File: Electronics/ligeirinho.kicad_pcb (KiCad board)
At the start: 2 copper layers, 76.1 x 55.1 mm, 27 parts, among them J1 Bateria, J10 ponte H2, J11 VS1838B, J12 MPU6050, J13 ADNS-9500, J14 ADNS-9500 3V3, J2 ESP32 esq, J3 ESP32 dir, J4 VL53L0X 1, J5 VL53L0X 2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

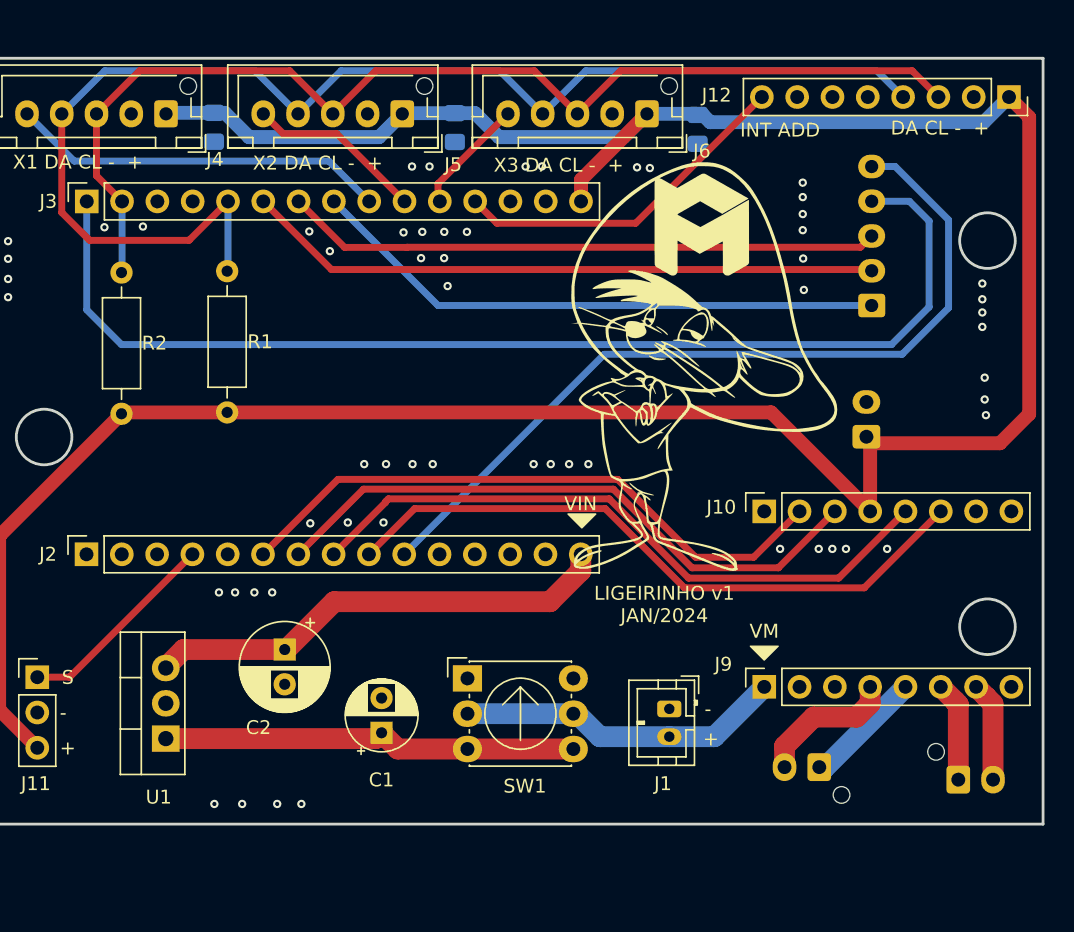
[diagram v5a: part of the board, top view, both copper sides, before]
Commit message: add: AMS1117 to 3v3 regulator
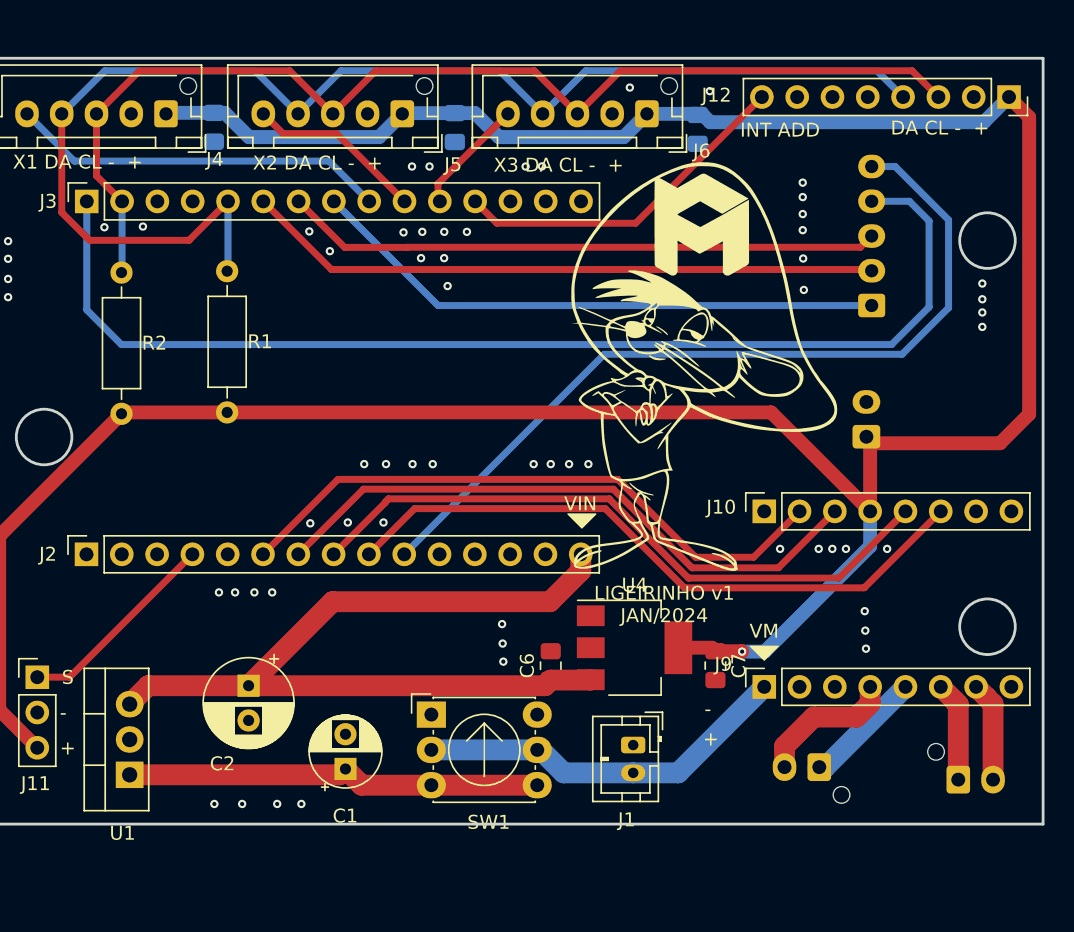
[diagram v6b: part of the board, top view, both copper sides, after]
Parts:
- added C6: 100nF, Capacitor_SMD:C_0805_2012Metric_Pad1.18x1.45mm_HandSolder, F.Cu at (195.1, 129.7)
- added C7: 10uF, Capacitor_SMD:C_0805_2012Metric_Pad1.18x1.45mm_HandSolder, F.Cu at (206.9, 129.7)
- added U4: AMS1117-3.3, Package_TO_SOT_SMD:SOT-223-3_TabPin2, F.Cu at (201.1, 128.4)
- moved J1 3.68 mm to (201.0, 135.4)
- moved C2 3.68 mm to (173.3, 131.1)
- moved U1 3.68 mm to (164.8, 137.6)
- moved C1 3.68 mm to (180.3, 137.1)
- moved SW1 3.68 mm to (186.5, 133.2)
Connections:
- J3 pad 15: 3V3 -> unconnected-(J3-Pin_15-Pad15)
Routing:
- net 5V: track 34.0 -> 62.4 mm
- net 3V3: track 199.0 -> 210.7 mm, vias 0 -> 1
- net 2s: track 23.5 -> 27.2 mm
- net GND: vias 56 -> 61
- net (no net): vias 2 -> 0

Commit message: fix: add some more stitching GND holes
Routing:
- net 3V3: track 210.7 -> 208.7 mm
- net BO1: track 7.18 -> 7.89 mm
- net GND: vias 61 -> 78

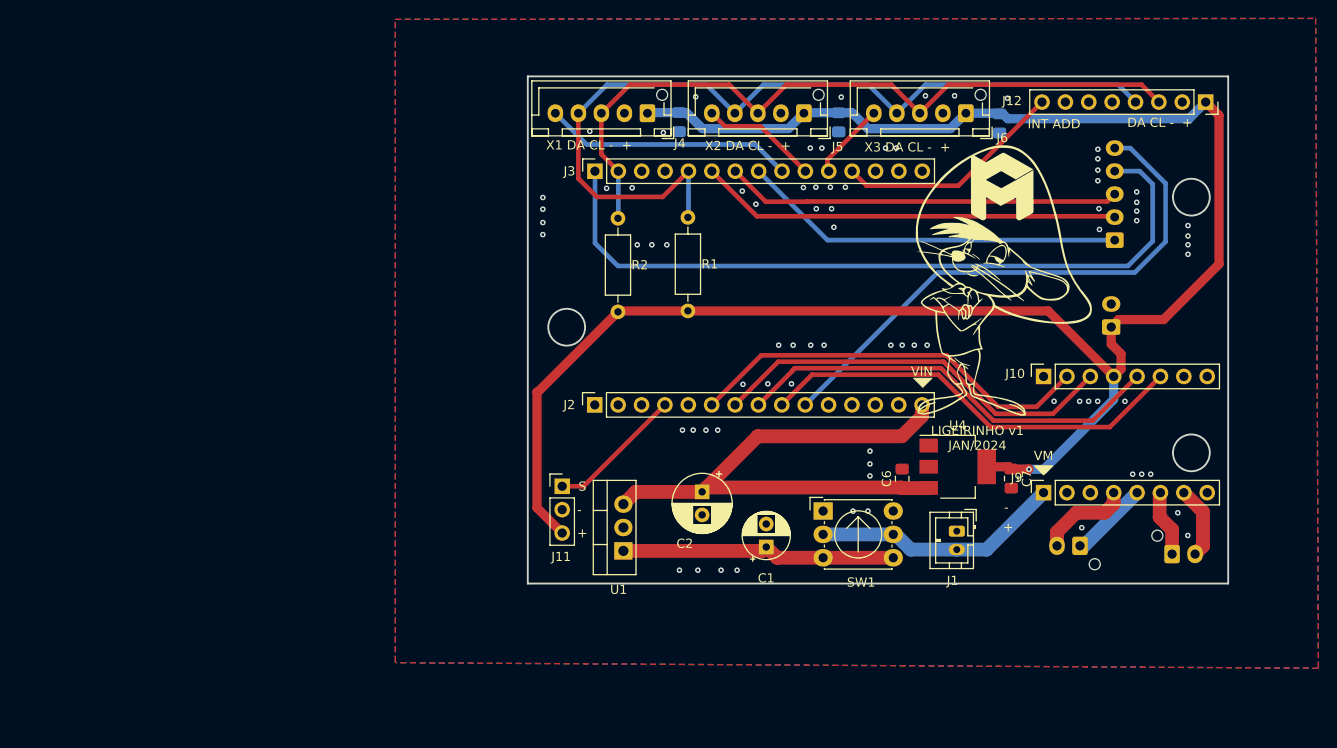
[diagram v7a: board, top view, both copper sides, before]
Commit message: chore: add mouse sensor to pcb and fix some measures
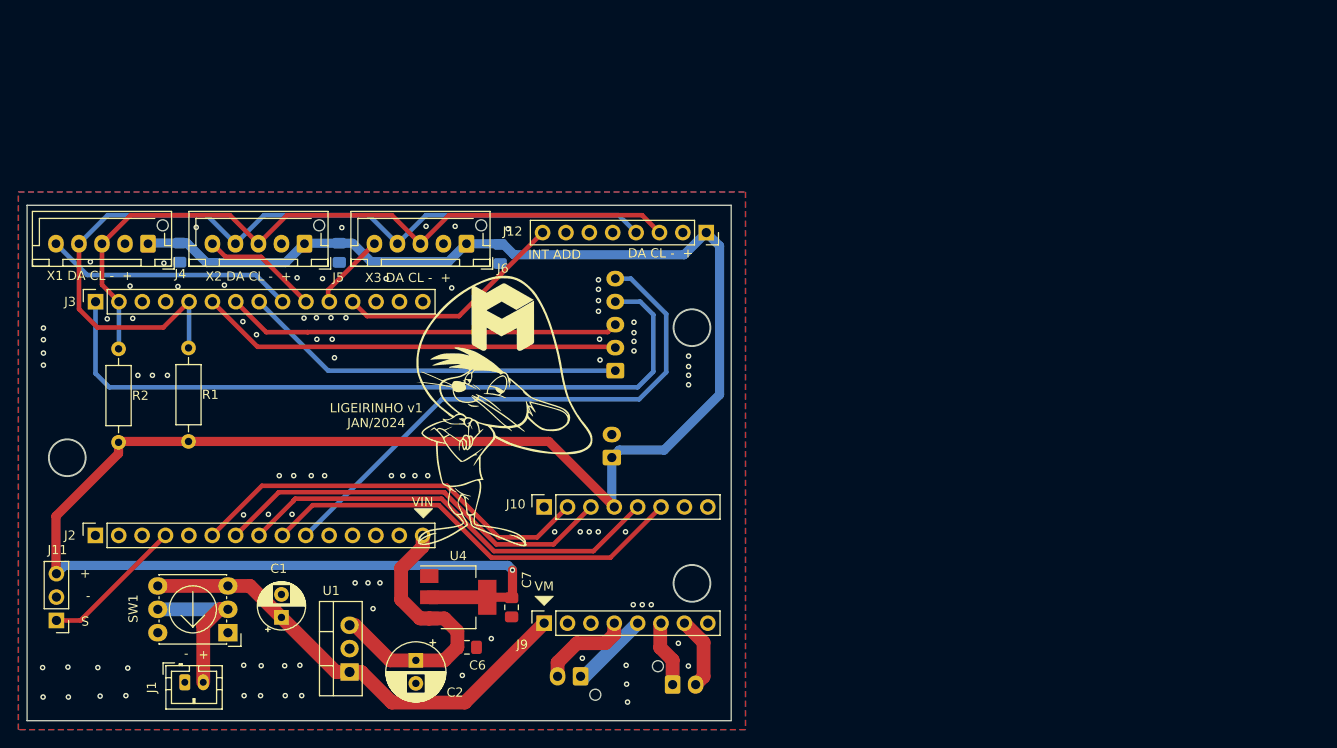
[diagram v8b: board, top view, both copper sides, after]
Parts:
- J10: value ponte H2 -> ponte H ld ESP
- J7: value MA -> Motor A
- J8: value MB -> Motor B
- J9: value ponte H1 -> ponte H ld motores
- moved J1 85.5 mm to (117.1, 151.8), turned to 0 degrees
- moved SW1 66.0 mm to (121.8, 146.4), turned to 180 degrees
- moved J11 56.9 mm to (103.2, 145.1), turned to 180 degrees
- moved G*** 56.5 mm to (171.8, 140.2)
- moved C4 56.1 mm to (133.9, 105.2)
- moved C5 56.1 mm to (151.4, 105.3)
- moved G*** 56.1 mm to (151.6, 122.3)
- moved J12 56.1 mm to (173.8, 103.0)
- moved J5 56.1 mm to (130.1, 104.2)
- moved J7 56.1 mm to (160.1, 151.2)
- moved J8 56.1 mm to (170.1, 152.1)
- moved U4 56.1 mm to (146.8, 142.6)
- moved G*** 56.1 mm to (125.5, 124.0)
- moved J2 56.1 mm to (107.4, 135.9)
- moved J4 56.1 mm to (113.1, 104.2)
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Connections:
- C1 pad 1: Net-(U1-VI) -> 2s
- J1 pad 2: 2s -> Net-(J1-Pin_2)
- SW1 pad 2: Net-(U1-VI) -> 2s
- SW1 pad 4: Net-(U1-VI) -> 2s
- SW1 pad C: 2s -> Net-(J1-Pin_2)
- U1 pad 1: Net-(U1-VI) -> 2s
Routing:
- net 5V: track 62.5 -> 31.1 mm
- net 3V3: track 208.7 -> 239.8 mm
- net Net-(U1-VI): track 30.0 -> 0.00 mm
- net 2s: track 27.2 -> 50.8 mm
- net Net-(J1-Pin_2): track 0.00 -> 17.2 mm
- net IR: track 14.8 -> 15.7 mm
- net MOSI sm: track 81.5 -> 80.6 mm
- net GND: vias 78 -> 93
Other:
- board size 76.1 x 55.1 mm -> 76.5 x 56 mm
